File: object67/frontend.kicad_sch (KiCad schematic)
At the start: 0 parts

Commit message: Analog frontend
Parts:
- added C24, C28, C30, C32, C42, C43, C46, C47, C50, C52, C54, C56: 10u, symbol Device:C_Polarized_Small
- added C27, C29, C31, C33, C44, C45, C48, C49, C51, C53, C55, C57: 0.1u, symbol Device:C_Small
- added C34, C36, C38, C40: 4.02n, symbol Device:C_Small
- added C35, C37, C39, C41: 1n, symbol Device:C_Small
- added IC4: TPA6120A2DWPR, object67:SOIC127P1040X275-21N, symbol object67:TPA6120A2DWPR
- added J1: SN37A12B, object67:SWITCHCRAFT_SN37A12B, symbol object67:SN37A12B
- added R10, R3, R4, R5, R6, R7, R8, R9: 2k, symbol Device:R_Small
- added R11, R14, R17, R20: 1.1k, symbol Device:R_Small
- added R12, R15, R18, R21: 619, symbol Device:R_Small
- added R13, R16, R19, R22: 1.1, symbol Device:R_Small
- added R23, R24, R25, R26, R27, R28, R29, R30: 1k, symbol Device:R_Small
- added R31, R32: 39.2, symbol Device:R_Small
- added U1, U2, U3, U4: OPA1612AxD, symbol Amplifier_Operational:OPA1612AxD
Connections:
- new net: R3.2, R4.1, U1.6 (-)
- new net: C38.1, R17.2, R18.1, R19.1
- new net: C40.1, R20.2, R21.1, R22.1
- new net: C39.1, R18.2, U3.6 (-)
- new net: C41.1, R21.2, U4.6 (-)
- new net: R8.2, R9.1, U2.1
- new net: R7.2, R8.1, U2.2 (-)
- new net: IC4.4 (LIN+), R27.2, R29.1
- new net: C34.1, R11.2, R12.1, R13.1
- new net: IC4.16 (RIN-), R24.1, R26.1
- new net: IC4.17 (RIN+), R23.1, R25.2
- new net: IC4.5 (LIN-), R28.1, R30.1
- new net: R10.1, R9.2, U2.6 (-)
- new net: C37.1, R15.2, U4.2 (-)
- new net: R3.1, R5.2, U1.1
- new net: C35.1, R12.2, U3.2 (-)
- new net: C36.1, R14.2, R15.1, R16.1
- new net: R5.1, R6.2, U1.2 (-)
- new net: J1.T, R32.2
- new net: J1.R, R31.1
- new net +15V: C24.1, C27.1, C30.1, C31.1, C42.1, C44.1, C46.1, C48.1, C50.1, C51.2, C52.1, C53.2, IC4.18 (RVCC+), IC4.3 (LVCC+), U1.8 (V+), U2.8 (V+), U3.8 (V+), U4.8 (V+)
- new net -15V: C28.2, C29.2, C32.2, C33.2, C43.2, C45.2, C47.2, C49.2, C54.1, C55.2, C56.1, C57.2, IC4.1 (LVCC-), IC4.20 (RVCC-), U1.4 (V-), U2.4 (V-), U3.4 (V-), U4.4 (V-)
- new net AOUTLN: R11.1
- new net AOUTLN2: C35.2, R13.2, R30.2, U1.3 (+), U3.1
- new net AOUTLP: R17.1
- new net AOUTLP2: C39.2, R19.2, R29.2, U1.5 (+), U3.7
- new net AOUTRN: R14.1
- new net AOUTRN2: C37.2, R16.2, R24.2, U2.3 (+), U4.1
- new net AOUTRP: R20.1
- new net AOUTRP2: C41.2, R22.2, R23.2, U2.5 (+), U4.7
- new net GNDA: C24.2, C27.2, C28.1, C29.1, C30.2, C31.2, C32.1, C33.1, C34.2, C36.2, C38.2, C40.2, C42.2, C43.1, C44.2, C45.1, C46.2, C47.1, C48.2, C49.1, C50.2, C51.1, C52.2, C53.1, C54.2, C55.1, C56.2, C57.1, IC4.21 (EP), J1.S, R25.1, R27.1, R6.1, R7.1, U3.3 (+), U3.5 (+), U4.3 (+), U4.5 (+)
- new net HOL: IC4.2 (LOUT), R28.2, R32.1
- new net HOR: IC4.19 (ROUT), R26.2, R31.2
- new net LL: R4.2, U1.7
- new net LR: R10.2, U2.7
- no-connect marks 0 -> 10
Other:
- note added: "Headphone Amplifier"
- note added: "MFB Filter"
- note added: "Power"
- note added: "Single Ended Conversion - Line Out"

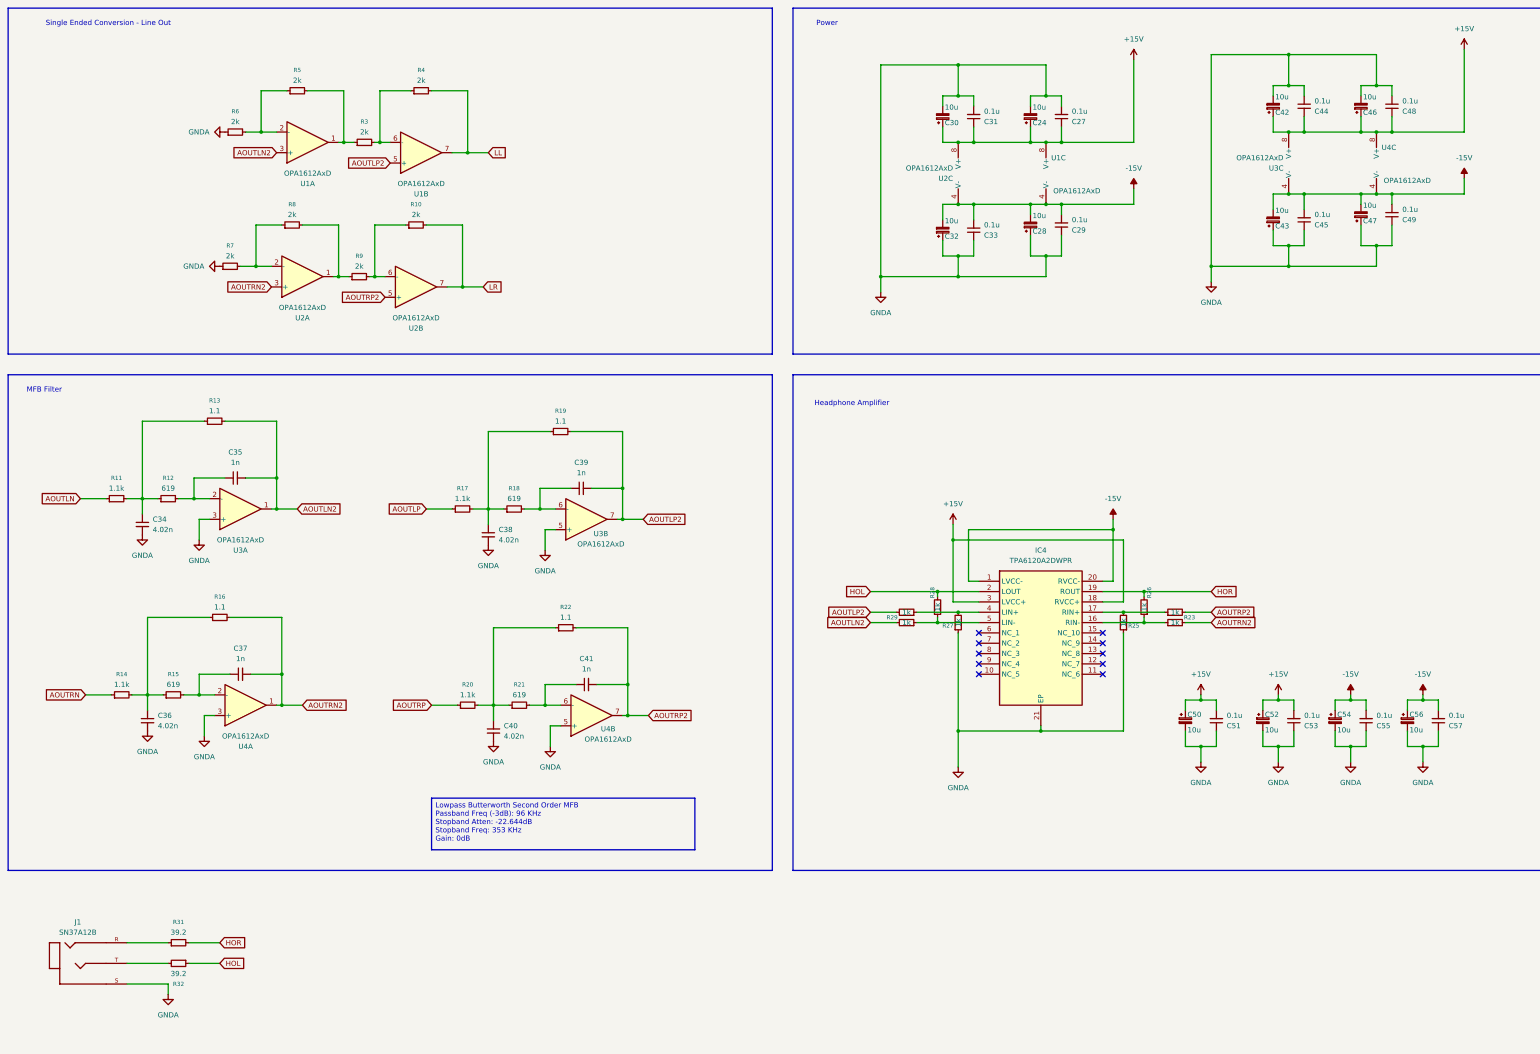
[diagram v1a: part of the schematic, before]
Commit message: Front end complete
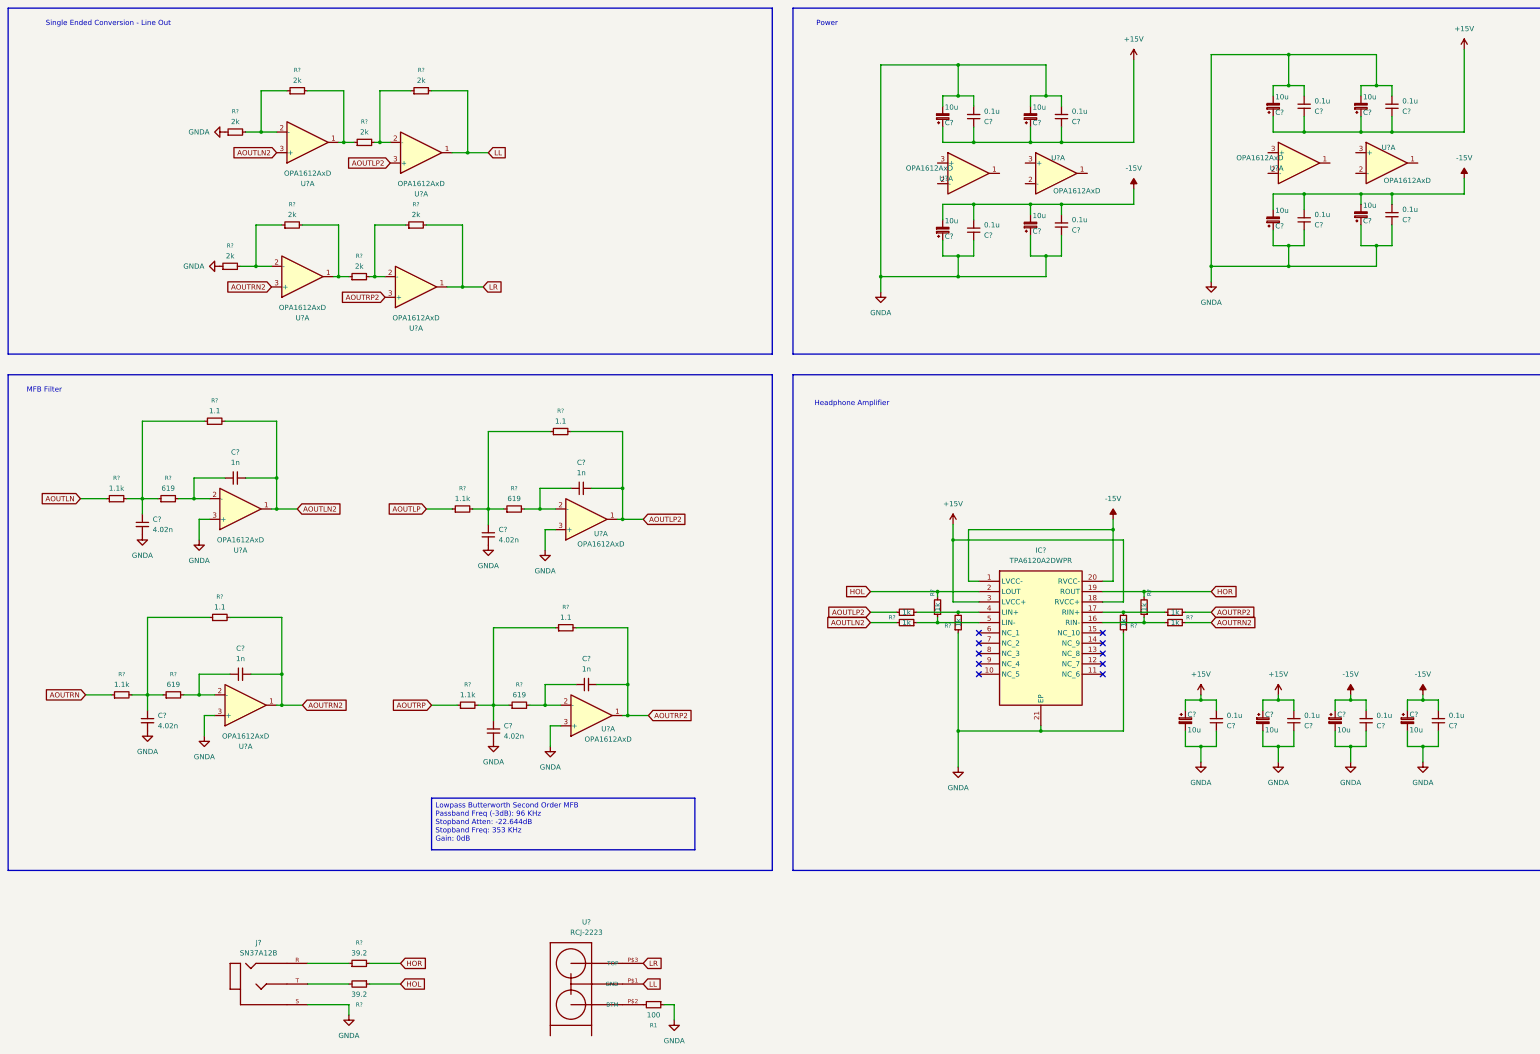
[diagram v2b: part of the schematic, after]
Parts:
- added R1: 100, symbol Device:R_Small
- added U?: RCJ-2223, object67:DUALRCA, symbol object67:RCJ-2223
- renumbered C42 to C?, C54 to C?, C41 to C?, C34 to C?, C51 to C?, C43 to C?, C37 to C?, C50 to C?, C44 to C?, C31 to C?, C46 to C?, C39 to C?, C49 to C?, C36 to C?, C56 to C?, C55 to C?, C27 to C?, C53 to C?, C30 to C?, C35 to C?, C57 to C?, C32 to C?, C52 to C?, C45 to C?, C48 to C?, C29 to C?, C40 to C?, C38 to C?, C24 to C?, C47 to C?, C28 to C?, C33 to C?, IC4 to IC?, J1 to J?, R19 to R?, R20 to R?, R18 to R?, R22 to R?, R27 to R?, R21 to R?, R10 to R?, R25 to R?, R11 to R?, R4 to R?, R13 to R?, R3 to R?, R14 to R?, R6 to R?, R24 to R?, R28 to R?, R9 to R?, R29 to R?, R32 to R?, R26 to R?, R12 to R?, R15 to R?, R5 to R?, R16 to R?, R30 to R?, R23 to R?, R17 to R?, R8 to R?, R7 to R?, R31 to R?, U1 to U?, U2 to U?, U3 to U?, U4 to U?
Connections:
- net +15V: no longer U?.8 (V+), U?.8 (V+), U?.8 (V+), U?.8 (V+)
- net -15V: no longer U?.4 (V-), U?.4 (V-), U?.4 (V-), U?.4 (V-)
- net AOUTLP2: now also U?.1, U?.3 (+); no longer U?.5 (+), U?.7
- net AOUTRP2: now also U?.1, U?.3 (+); no longer U?.5 (+), U?.7
- net GNDA: now also U?.3 (+), U?.3 (+), R1.1; no longer U?.5 (+), U?.5 (+)
- net LL: now also U?.1, U?.P$1 (GND); no longer U?.7
- net LR: now also U?.1, U?.P$3 (TOP); no longer U?.7
- net at R?.1, R?.2: now also U?.2 (-); no longer U?.6 (-) (x2)
- net at C?.1, R?.2: now also U?.2 (-); no longer U?.6 (-) (x2)
- new net: R1.2, U?.P$2 (BTM)
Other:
- moved on the sheet: J?, R?

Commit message: KiCad crashed
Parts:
- removed U? (x12): OPA1612AxD, symbol Amplifier_Operational:OPA1612AxD
- added U1, U2, U3, U4: OPA1612AxD, symbol Amplifier_Operational:OPA1612AxD
- gave numbers to parts that had none: 65
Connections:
- net +15V: now also U1.8 (V+), U2.8 (V+), U3.8 (V+), U4.8 (V+)
- net -15V: now also U1.4 (V-), U2.4 (V-), U3.4 (V-), U4.4 (V-)
- net AOUTLN2: now also U1.3 (+), U3.1
- net AOUTLP2: now also U1.5 (+), U3.7
- net AOUTRN2: now also U2.3 (+), U4.1
- net AOUTRP2: now also U2.5 (+), U4.7
- net GNDA: now also U3.3 (+), U3.5 (+), U4.3 (+), U4.5 (+)
- net LL: now also U1.7
- net LR: now also U2.7
- net at R15.2, R17.1: now also U1.6 (-)
- net at C7.1, R20.2: now also U3.6 (-)
- net at C8.1, R21.2: now also U4.6 (-)
- net at R10.2, R12.1: now also U2.1
- net at R10.1, R8.2: now also U2.2 (-)
- net at R12.2, R16.1: now also U2.6 (-)
- net at C4.1, R5.2: now also U4.2 (-)
- net at R11.2, R15.1: now also U1.1
- net at C3.1, R4.2: now also U3.2 (-)
- net at R11.1, R9.2: now also U1.2 (-)

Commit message: KiCad crashed x2
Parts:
- removed U1: OPA1612AxD, symbol Amplifier_Operational:OPA1612AxD
- added U6: OPA1612AxD, symbol Amplifier_Operational:OPA1612AxD
- R34: renamed from R1; value 100 -> 10
- renumbered C13 to C24, C15 to C27, C14 to C28, C16 to C29, C9 to C30, C11 to C31, C10 to C32, C12 to C33, C1 to C34, C3 to C35, C2 to C36, C4 to C37, C5 to C38, C7 to C39, C6 to C40, C8 to C41, C20 to C42, C21 to C43, C23 to C44, C24 to C45, C26 to C46, C27 to C47, C29 to C48, C30 to C49, C17 to C50, C18 to C51, C19 to C52, C22 to C53, C25 to C54, C28 to C55, C31 to C56, C32 to C57, IC1 to IC4, R16 to R10, R2 to R11, R4 to R12, R6 to R13, R3 to R14, R5 to R15, R7 to R16, R18 to R17, R20 to R18, R22 to R19, R19 to R20, R23 to R22, R30 to R23, R31 to R24, R28 to R25, R29 to R26, R26 to R28, R24 to R29, R15 to R3, R25 to R30, R13 to R31, R14 to R32, R17 to R4, R11 to R5, R9 to R6, R8 to R7, R10 to R8, R12 to R9, U9 to U5
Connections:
- net +15V: now also U6.8 (V+)
- net -15V: now also U6.4 (V-)
- net AOUTLN2: now also U2.3 (+), U4.1; no longer U3.1
- net AOUTLP2: now also U2.5 (+), U4.7; no longer U3.7
- net AOUTRN2: now also U3.3 (+), U6.1; no longer U2.3 (+), U4.1
- net AOUTRP2: now also U3.5 (+), U6.7; no longer U2.5 (+), U4.7
- net GNDA: now also U6.3 (+), U6.5 (+); no longer U3.3 (+), U3.5 (+)
- net LL: now also U2.7
- net LR: now also U3.7; no longer U2.7
- net at C39.1, R18.2: now also U4.6 (-); no longer U3.6 (-)
- net at C41.1, R21.2: now also U6.6 (-); no longer U4.6 (-)
- net at C37.1, R15.2: now also U6.2 (-); no longer U4.2 (-)
- net at R10.1, R9.2: now also U3.6 (-); no longer U2.6 (-)
- net at R3.2, R4.1: now also U2.6 (-)
- net at C35.1, R12.2: now also U4.2 (-); no longer U3.2 (-)
- net at R3.1, R5.2: now also U2.1
- net at R5.1, R6.2: now also U2.2 (-)
- net at R8.2, R9.1: now also U3.1; no longer U2.1
- net at R7.2, R8.1: now also U3.2 (-); no longer U2.2 (-)

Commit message: ????
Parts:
- added unit 2 of U6
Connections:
- net AOUTRP2: now also U6.7; no longer U6.7
- net GNDA: now also U6.5 (+); no longer U6.5 (+)
- net at C41.1, R21.2: now also U6.6 (-); no longer U6.6 (-)

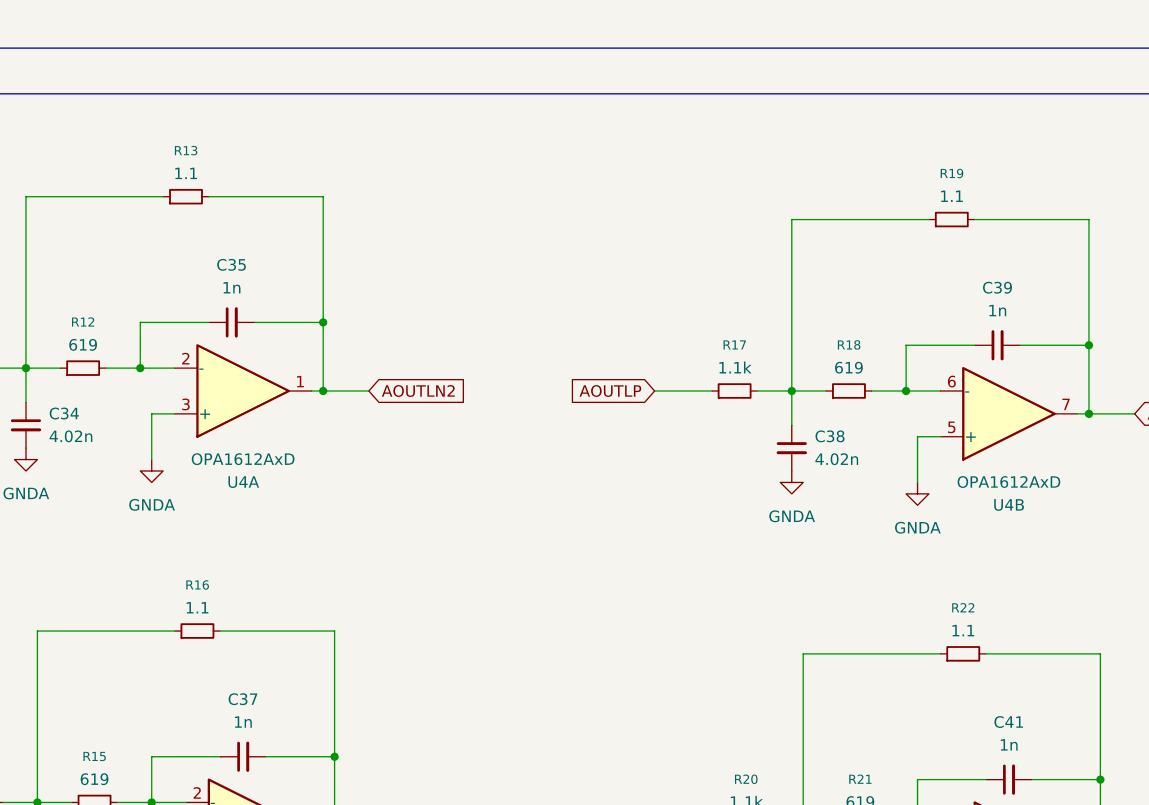
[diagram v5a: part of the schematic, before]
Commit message: Update feedback resistor value
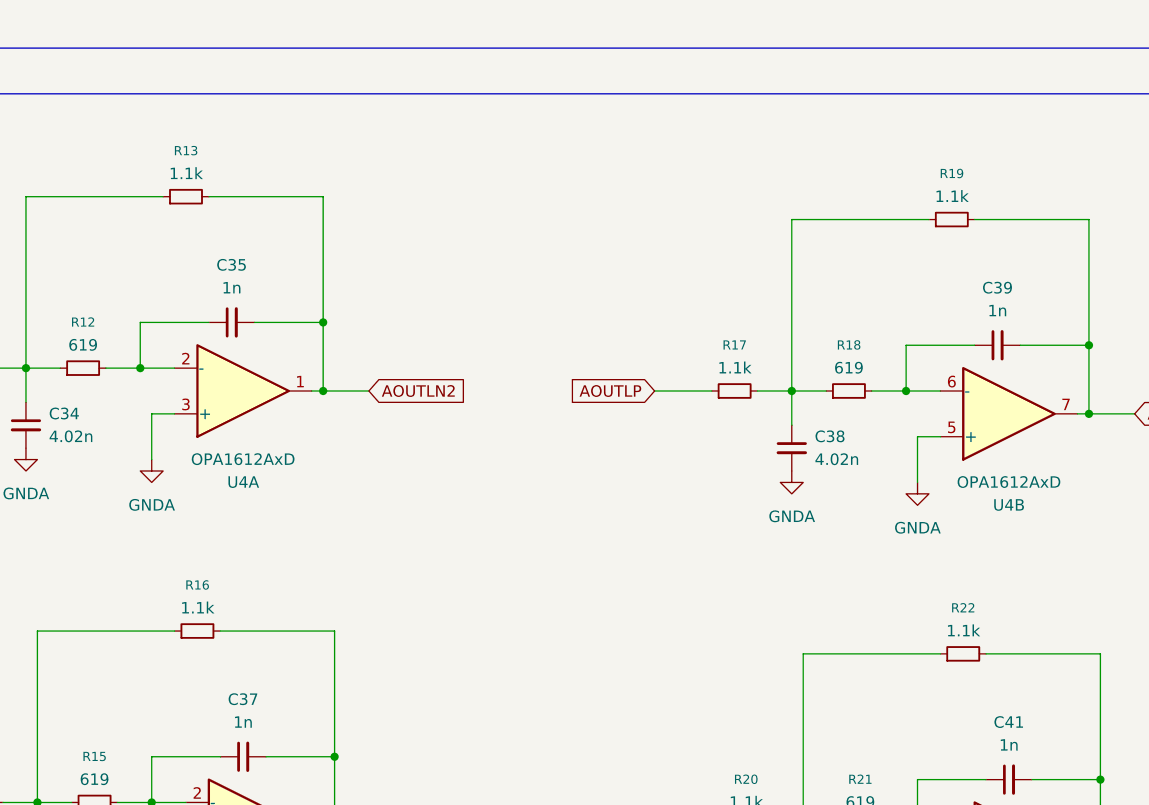
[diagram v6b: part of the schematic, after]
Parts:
- R13, R16, R19, R22: value 1.1 -> 1.1k
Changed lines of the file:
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@@
 			)
 		)
-		(property "Value" "1.1"
+		(property "Value" "1.1k"
 			(at 152.4 115.57 90)
 			(effects
@@
 			)
 		)
-		(property "Value" "1.1"
+		(property "Value" "1.1k"
 			(at 153.67 163.83 90)
 			(effects
@@
 			)
 		)
-		(property "Value" "1.1"
+		(property "Value" "1.1k"
 			(at 67.31 113.03 90)
 			(effects
@@
 			)
 		)
-		(property "Value" "1.1"
+		(property "Value" "1.1k"
 			(at 68.58 161.29 90)
 			(effects
